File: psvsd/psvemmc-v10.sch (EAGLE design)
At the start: 40 parts, among them U1 USB2244QFN, U2 LP3996_DSC_10, U3 LSF0204RUTR, U4 LSF0204RUTR, U5 LSF0204RUTR, X1 ZX62D-B-5PA8, Y1 XRCGB

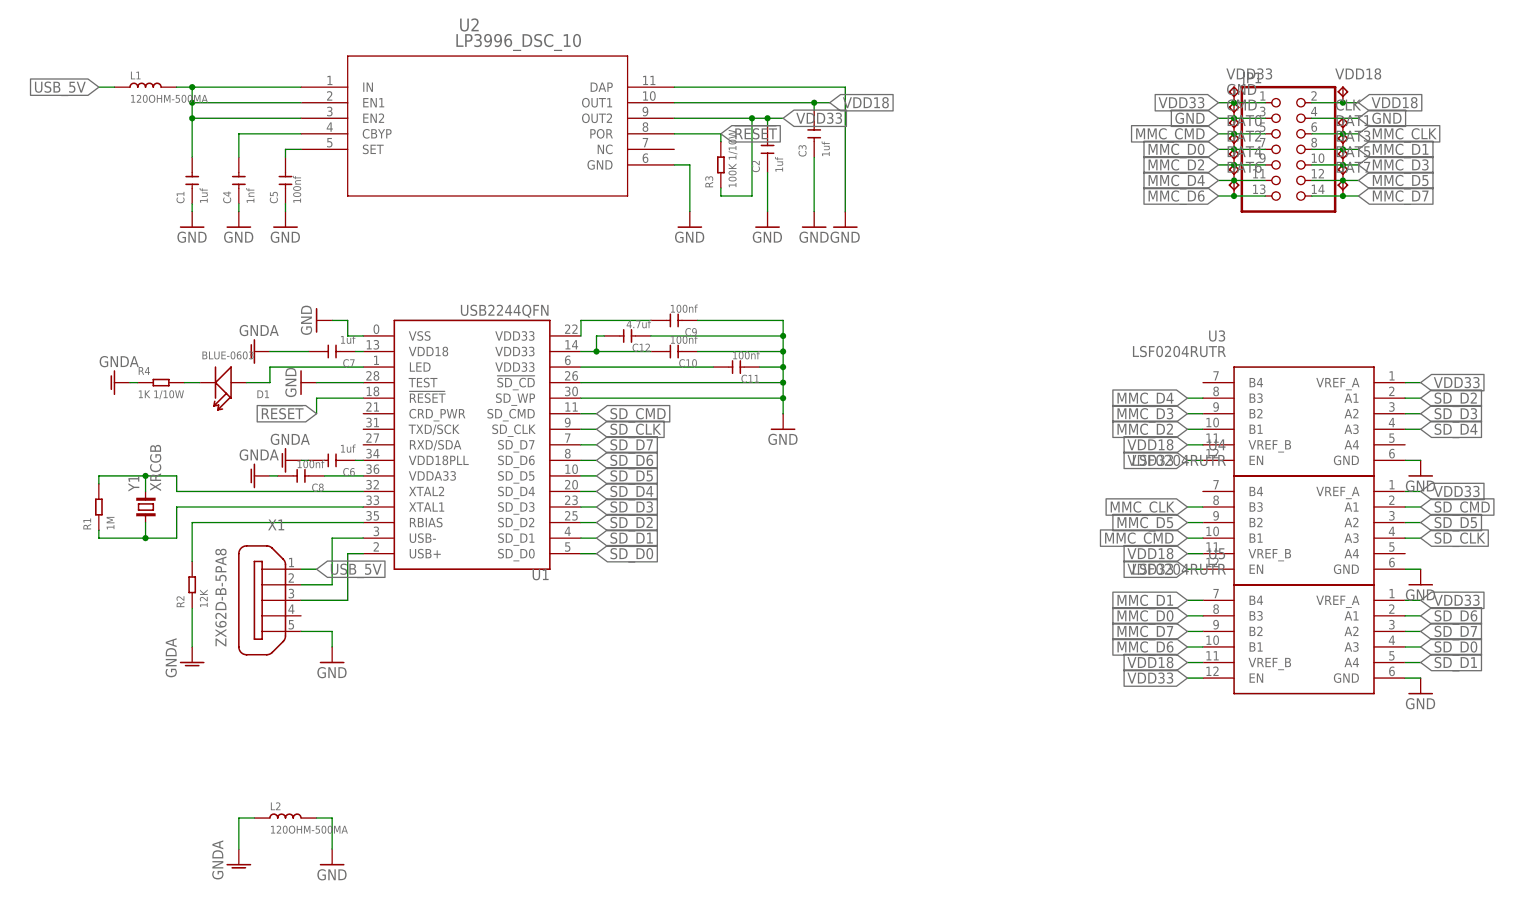
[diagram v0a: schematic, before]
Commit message: psvemmc v1.1: fixed missing caps for crystal and fixed direction of translator
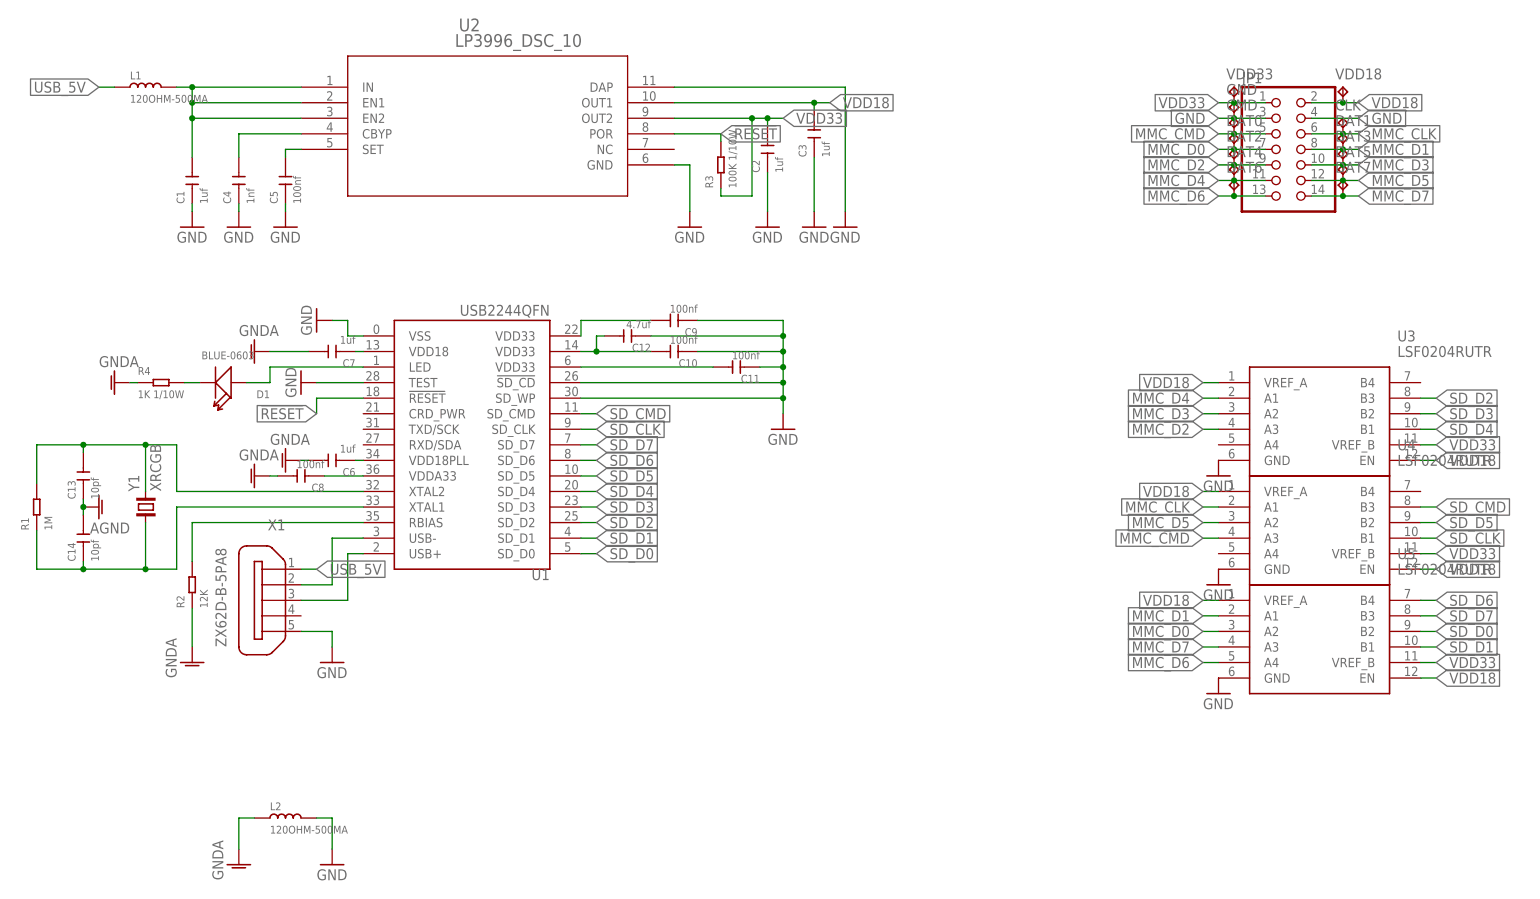
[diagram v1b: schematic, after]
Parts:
- added C13, C14: 10pf, Seeed-Capacitor:CERAMIC-10PF-50V-5%-NPO(0603)
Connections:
- net GNDA: now also C13.1, C14.2
- net MMC_CLK: now also U4.A1; no longer U4.B3
- net MMC_CMD: now also U4.A3; no longer U4.B1
- net MMC_D0: now also U5.A2; no longer U5.B3
- net MMC_D1: now also U5.A1; no longer U5.B4
- net MMC_D2: now also U3.A3; no longer U3.B1
- net MMC_D3: now also U3.A2; no longer U3.B2
- net MMC_D4: now also U3.A1; no longer U3.B3
- net MMC_D5: now also U4.A2; no longer U4.B2
- net MMC_D6: now also U5.A4; no longer U5.B1
- net MMC_D7: now also U5.A3; no longer U5.B2
- net SD_CLK: now also U4.B1; no longer U4.A3
- net SD_CMD: now also U4.B3; no longer U4.A1
- net SD_D0: now also U5.B2; no longer U5.A3
- net SD_D1: now also U5.B1; no longer U5.A4
- net SD_D2: now also U3.B3; no longer U3.A1
- net SD_D3: now also U3.B2; no longer U3.A2
- net SD_D4: now also U3.B1; no longer U3.A3
- net SD_D5: now also U4.B2; no longer U4.A2
- net SD_D6: now also U5.B4; no longer U5.A1
- net SD_D7: now also U5.B3; no longer U5.A2
- net VDD18: now also U3.EN, U3.VREF_A, U4.EN, U4.VREF_A, U5.EN, U5.VREF_A; no longer U3.VREF_B, U4.VREF_B, U5.VREF_B
- net VDD33: now also U3.VREF_B, U4.VREF_B, U5.VREF_B; no longer U3.EN, U3.VREF_A, U4.EN, U4.VREF_A, U5.EN, U5.VREF_A
- net XTAL1: now also C14.1
- net XTAL2: now also C13.2
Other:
- moved on the sheet: R1, U3, U4, U5
